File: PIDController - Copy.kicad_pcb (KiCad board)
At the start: 2 copper layers, 100 x 100 mm, 26 parts, among them J1 Jack-DC, J2 Jack-DC, J4 Jack-DC, J5 Jack-DC, M1 Motor_DC, Q1 BD433, Q2 BD434, U1 LM324, U2 LM324

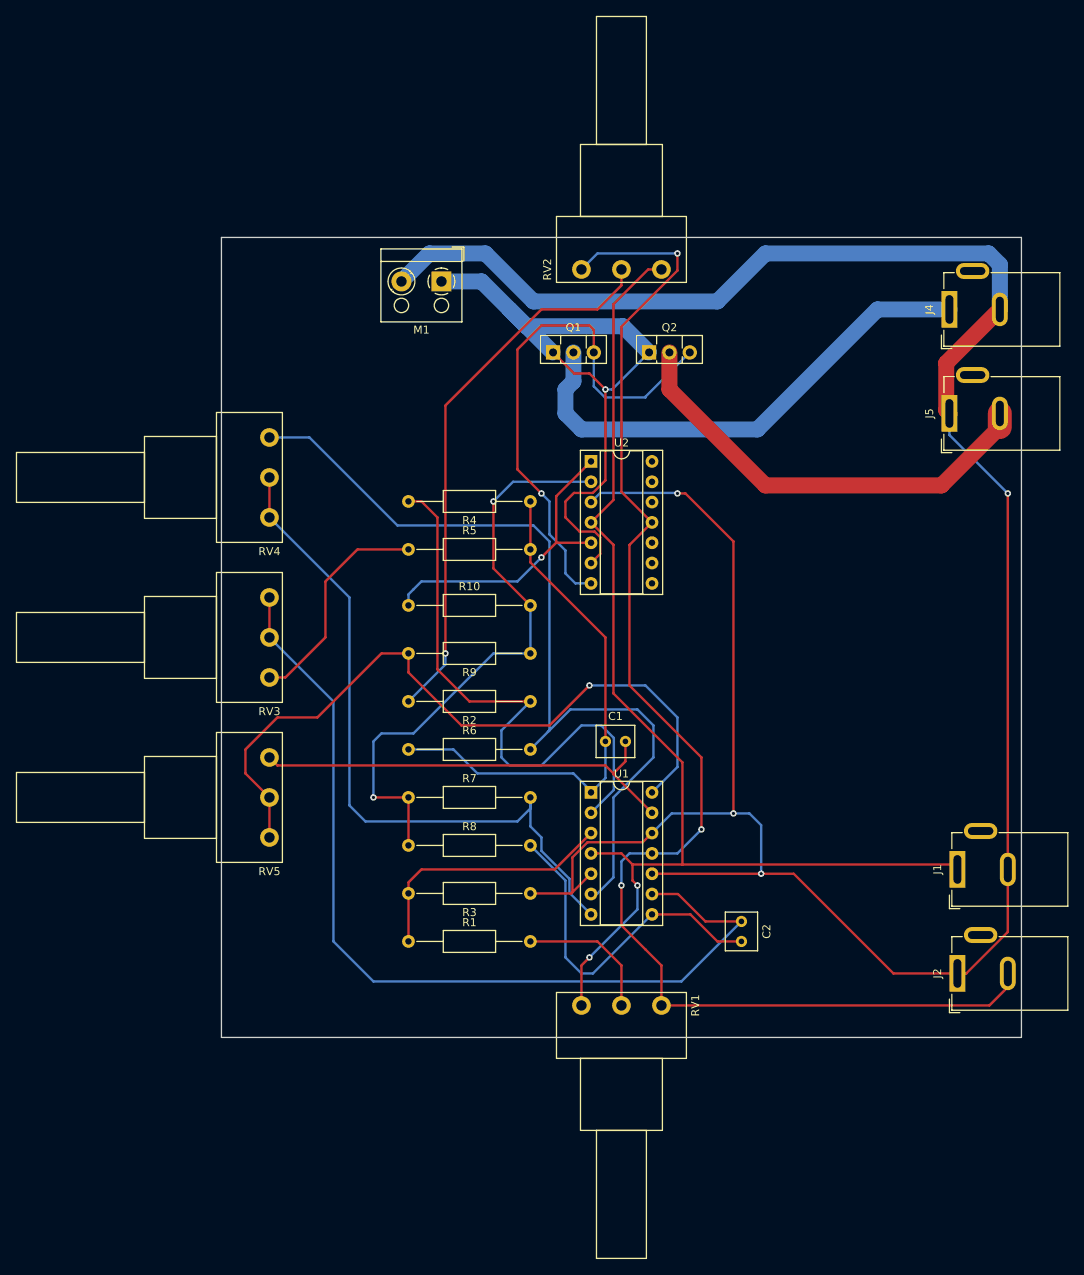
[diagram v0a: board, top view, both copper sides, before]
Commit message: improved the general design, added ground plane, silkmask etc.
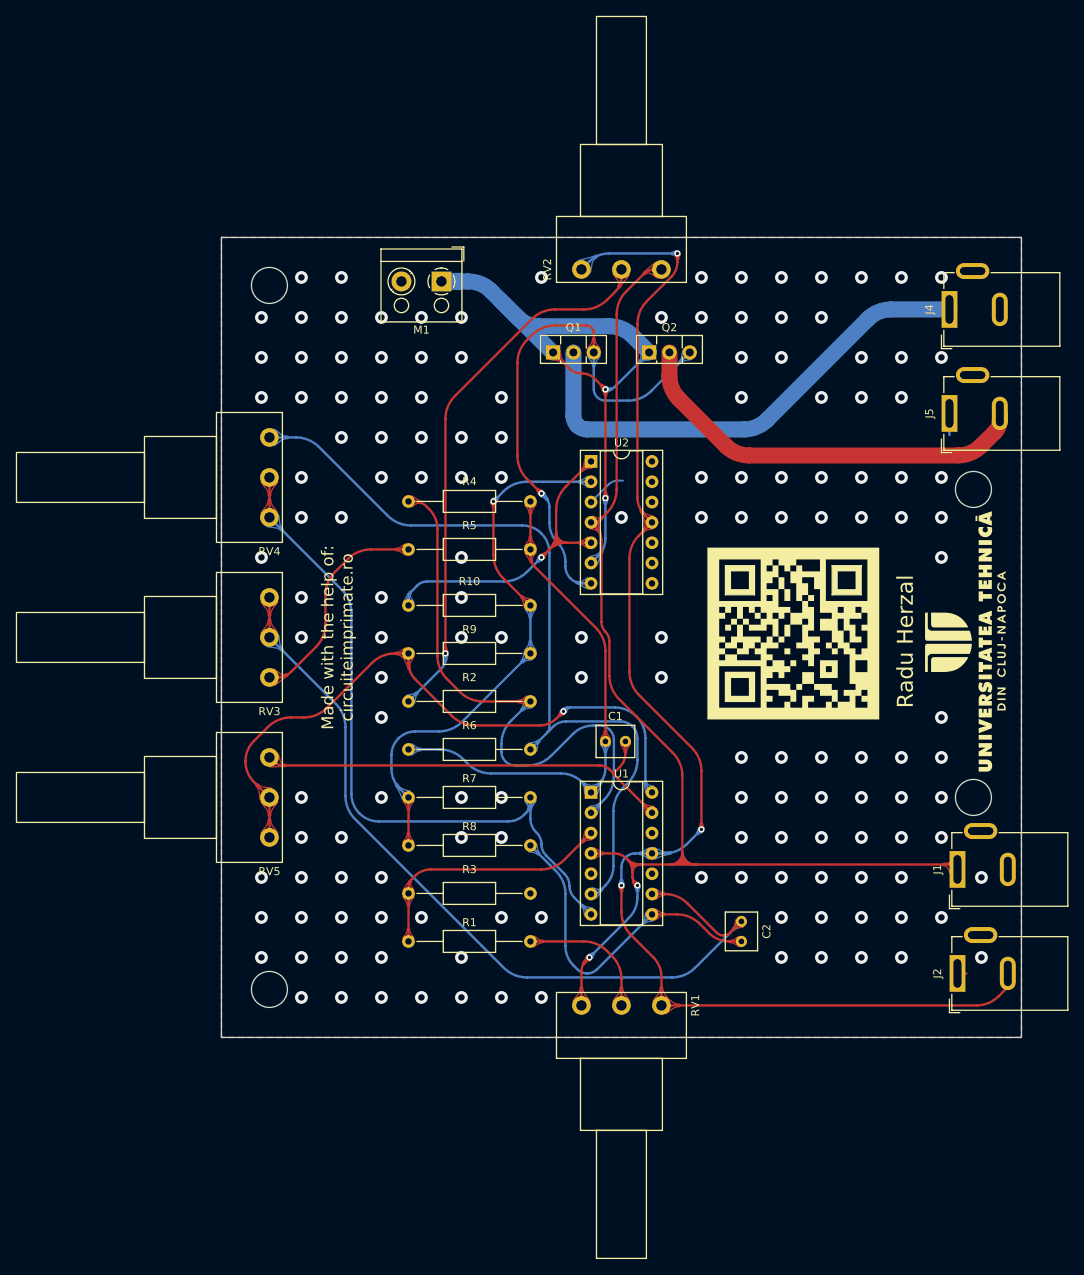
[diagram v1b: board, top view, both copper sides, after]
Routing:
- net GND: track 323.3 -> 8.84 mm, vias 4 -> 152
- net Net-(C2-Pad1): track 115.1 -> 104.5 mm
- net Net-(R9-Pad2): track 90.8 -> 81.0 mm
- net Net-(R10-Pad2): track 75.7 -> 68.6 mm, vias 2 -> 1
- net Net-(R6-Pad2): track 107.3 -> 101.3 mm
- net MotorInput: track 81.6 -> 76.6 mm, vias 1 -> 2
- net +12V: track 151.1 -> 155.0 mm
- net -12V: track 171.9 -> 168.0 mm
- net Net-(J5-Pad2): track 55.6 -> 51.8 mm
- net Net-(R10-Pad1): track 38.8 -> 41.3 mm
- net Net-(R2-Pad1): track 72.9 -> 71.5 mm
- net Net-(R7-Pad2): track 88.4 -> 87.0 mm
- net Net-(J4-Pad1): track 63.1 -> 61.7 mm
- net Net-(C1-Pad1): track 66.2 -> 65.0 mm
- net Net-(C2-Pad2): track 43.1 -> 42.2 mm
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- added copper zone on B.Cu, net GND
- added copper zone on F.Cu, net GND
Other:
- outline, holes or cut-outs redrawn
- board text added: "Made with the help of: circuiteimprimate.ro"
- board text added: "Radu Herzal"
- board text added: "{ "ViaStitching": "0.1", "stitch_zone_0": { "HSpacing": "5", "VSpacing": "5", "Clearance": "0.5", "Randomize": false } }"

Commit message: changed sponsor link
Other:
- board text added: "Made with the help of: circuite-imprimate.ro"
- board text removed: "Made with the help of: circuiteimprimate.ro"
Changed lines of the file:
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@@
     (effects (font (size 2 2) (thickness 0.3)))
   )
-  (gr_text "Made with the help of:\ncircuiteimprimate.ro\n" (at 31.5 67 90) (layer "F.SilkS")
+  (gr_text "Made with the help of:\ncircuite-imprimate.ro\n" (at 31.5 67 90) (layer "F.SilkS")
     (effects (font (size 1.5 1.5) (thickness 0.15)))
   )
